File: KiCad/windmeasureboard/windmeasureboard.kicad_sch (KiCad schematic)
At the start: 9 parts, among them J1 ESQ-120-XX-X-D-XX, U1 ESP32-S2-DEVKITC-1, U2 LM1084ISX-5.0_NOPB

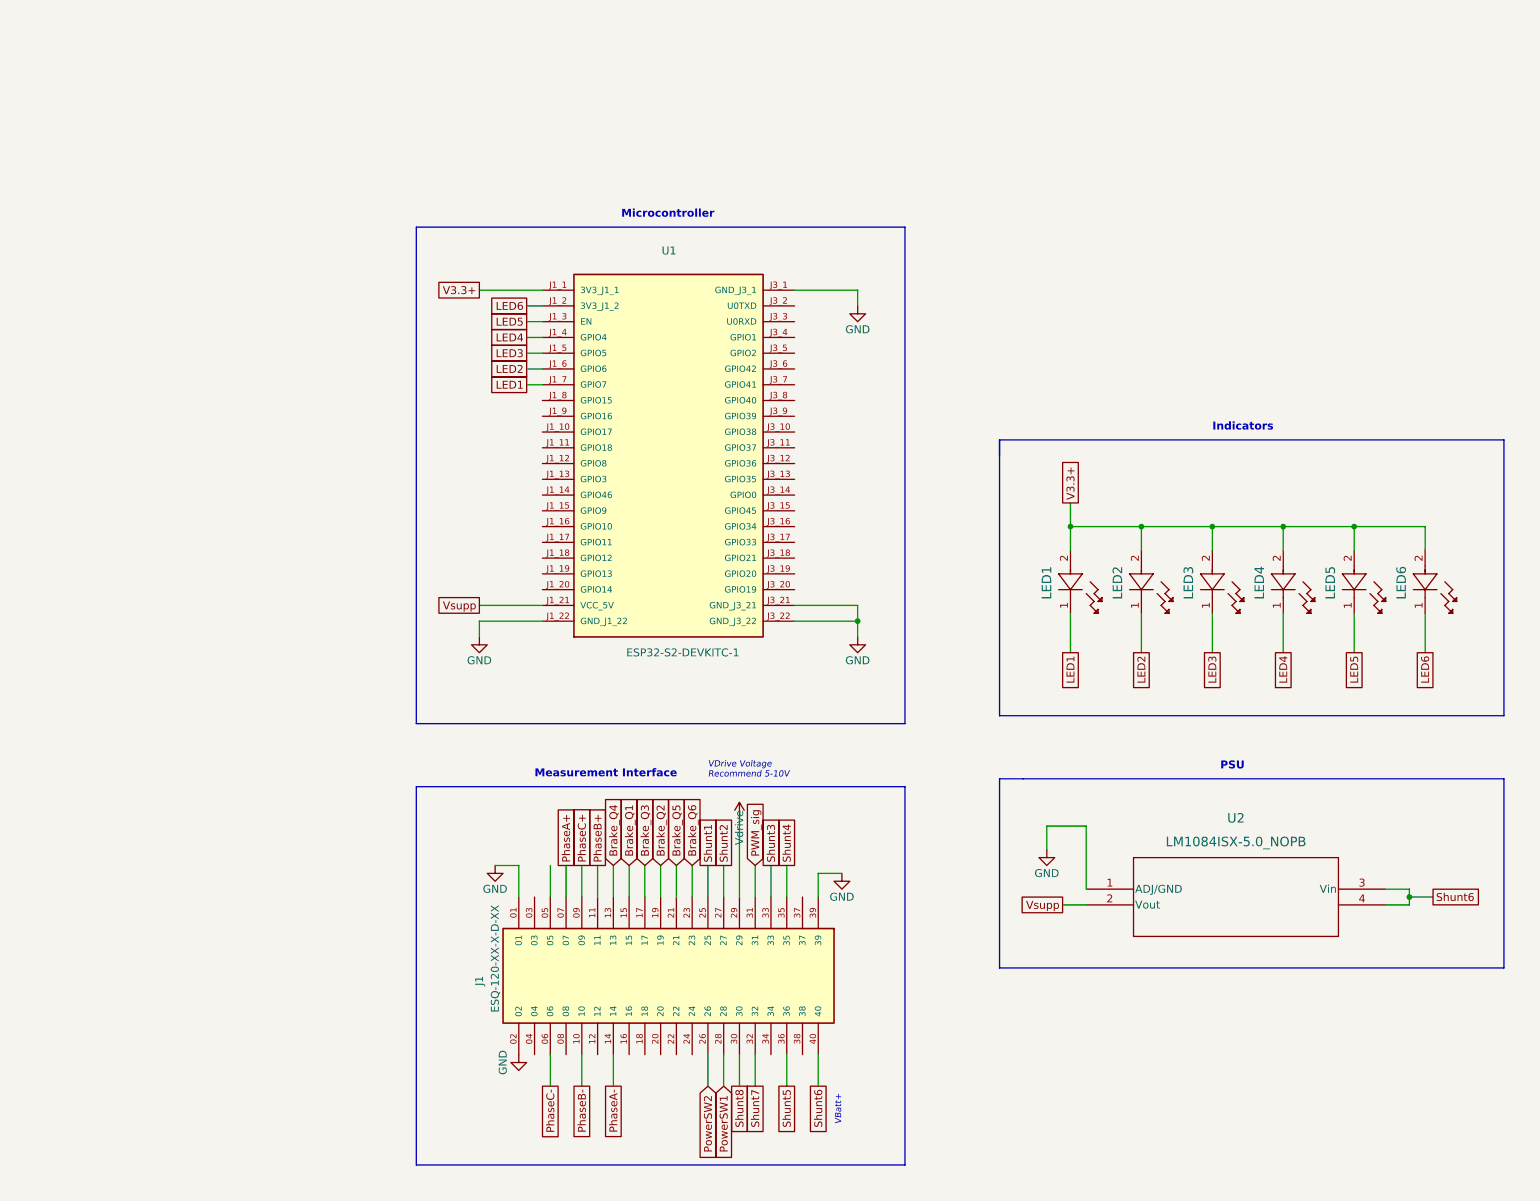
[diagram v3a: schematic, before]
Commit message: V1 Measure Board Finished
Also started manual data collection for turbine and started updating files to kicad V7
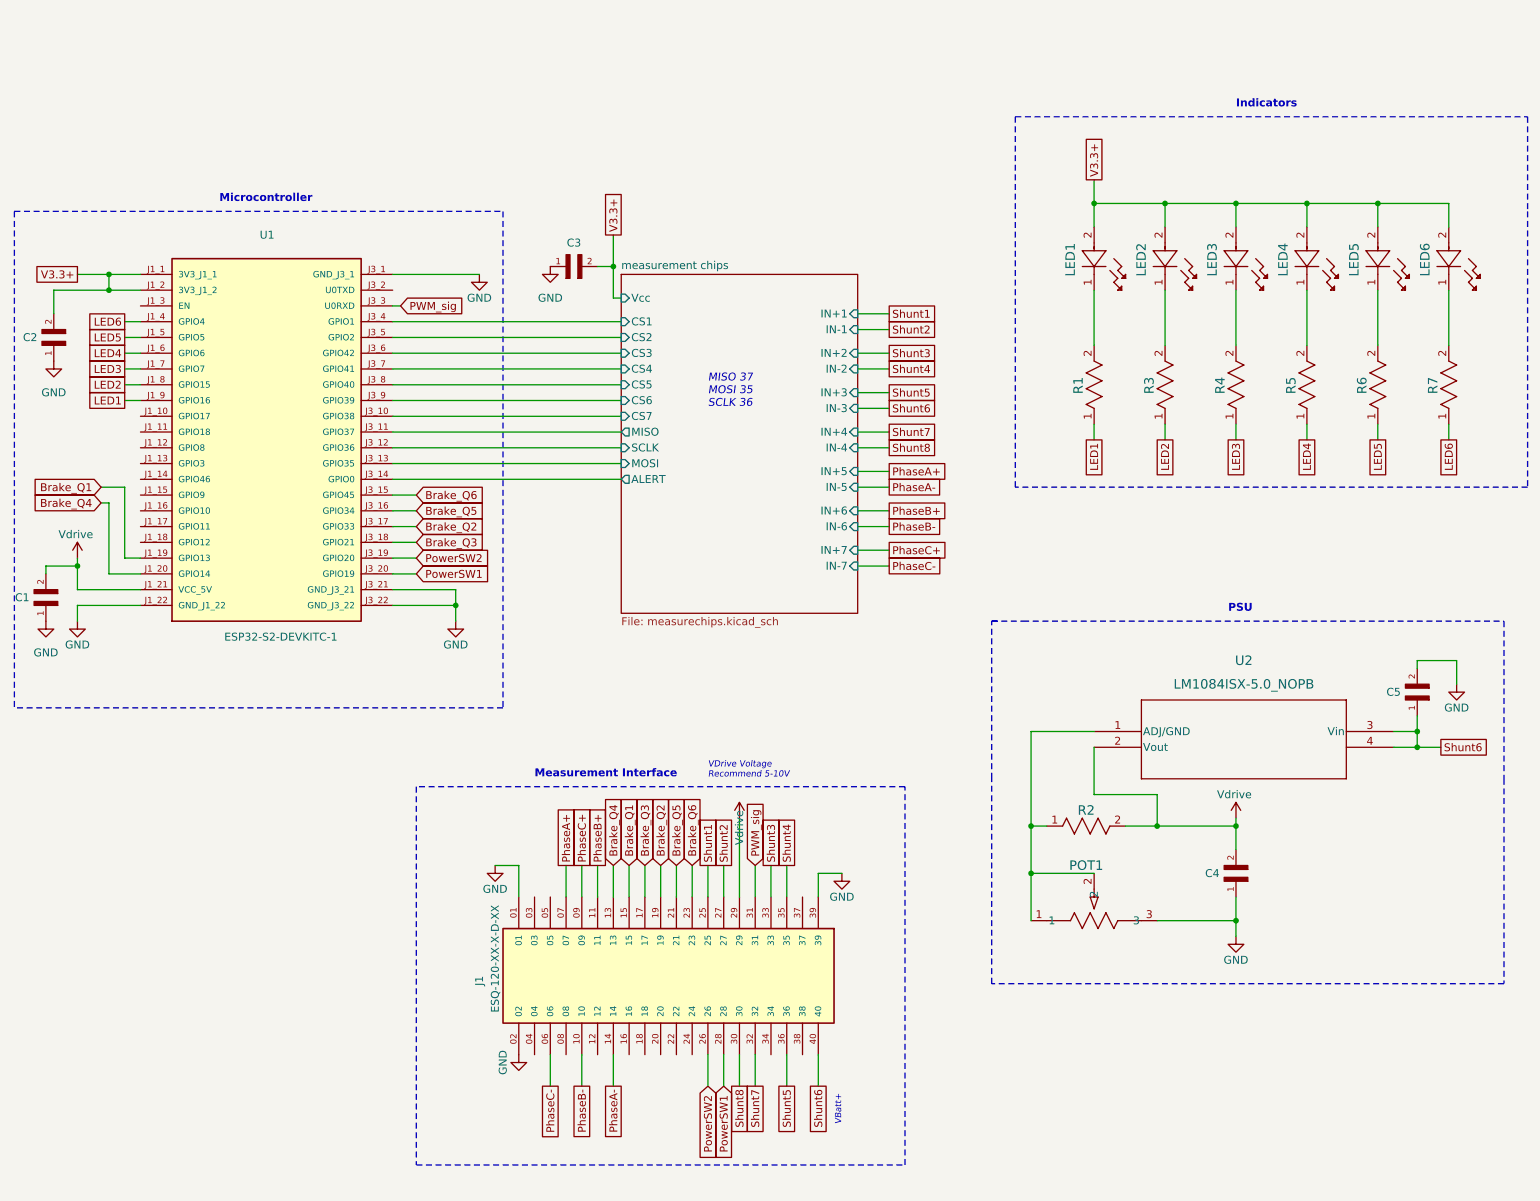
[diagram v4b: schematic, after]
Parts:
- added C1, C2, C3, C4, C5: GRM32EC72A106KE05L, footprints:CAPC3225X270N, symbol GRM32EC72A106KE05L:GRM32EC72A106KE05L
- added POT1: 3296Y-1-502LF, footprints:POT_3296Y, symbol 3296Y-1-502LF:3296Y-1-502LF
- added R1, R3, R4, R5, R6, R7: ERJXGNJ560Y, ERJXGN_RCD, symbol ERJXGNJ560Y:ERJXGNJ560Y
- added R2: CRCW04021K00FKED, footprints:RES_CRCW_0402, symbol CRCW04021K00FKED:CRCW04021K00FKED
- LED1, LED2, LED3, LED4, LED5, LED6: footprint LED_XZMG56W_SLD -> footprints:LED_XZMG56W_SLD
- U2: footprint TS3B -> footprints:TS3B
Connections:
- net Vsupp is gone; now on net Vdrive: U1.J1_21 (VCC_5V), U2.2 (Vout)
- net Brake_Q1: now also U1.J1_19 (GPIO13)
- net Brake_Q2: now also U1.J3_17 (GPIO33)
- net Brake_Q3: now also U1.J3_18 (GPIO21)
- net Brake_Q4: now also U1.J1_20 (GPIO14)
- net Brake_Q5: now also U1.J3_16 (GPIO34)
- net Brake_Q6: now also U1.J3_15 (GPIO45)
- net GND: now also C1.1, C2.1, C3.1, C4.1, C5.2, POT1.3; no longer U2.1 (ADJ/GND)
- net LED1: now also U1.J1_9 (GPIO16), R1.1; no longer LED1.1, U1.J1_7 (GPIO7)
- net LED2: now also U1.J1_8 (GPIO15), R3.1; no longer LED2.1, U1.J1_6 (GPIO6)
- net LED3: now also U1.J1_7 (GPIO7), R4.1; no longer LED3.1, U1.J1_5 (GPIO5)
- net LED4: now also U1.J1_6 (GPIO6), R5.1; no longer LED4.1, U1.J1_4 (GPIO4)
- net LED5: now also U1.J1_5 (GPIO5), R6.1; no longer LED5.1, U1.J1_3 (EN)
- net LED6: now also U1.J1_4 (GPIO4), R7.1; no longer LED6.1, U1.J1_2 (3V3_J1_2)
- net PWM_sig: now also U1.J3_3 (U0RXD)
- net PowerSW1: now also U1.J3_20 (GPIO19)
- net PowerSW2: now also U1.J3_19 (GPIO20)
- net Shunt6: now also C5.1
- net V3.3+: now also U1.J1_2 (3V3_J1_2), C2.2, C3.2
- net Vdrive: now also C1.2, C4.2, R2.2
- net measurement chips/CS7: now reaches U1.J3_10 (GPIO38)
- net measurement chips/MISO: now reaches U1.J3_11 (GPIO37)
- net measurement chips/SCLK: now reaches U1.J3_12 (GPIO36)
- net measurement chips/MOSI: now reaches U1.J3_13 (GPIO35)
- net measurement chips/ALERT: now reaches U1.J3_14 (GPIO0)
- net measurement chips/CS1: now reaches U1.J3_4 (GPIO1)
- net measurement chips/CS2: now reaches U1.J3_5 (GPIO2)
- net measurement chips/CS3: now reaches U1.J3_6 (GPIO42)
- net measurement chips/CS4: now reaches U1.J3_7 (GPIO41)
- net measurement chips/CS5: now reaches U1.J3_8 (GPIO40)
- net measurement chips/CS6: now reaches U1.J3_9 (GPIO39)
- new net: LED5.1, R6.2
- new net: LED2.1, R3.2
- new net: LED3.1, R4.2
- new net: POT1.1, POT1.2, R2.1, U2.1 (ADJ/GND)
- new net: LED6.1, R7.2
- new net: LED4.1, R5.2
- new net: LED1.1, R1.2
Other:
- added sheet measurement chips (measurechips.kicad_sch)
- note added: "MISO 37 MOSI 35 SCLK 36"
- moved on the sheet: LED1, LED2, LED3, LED4, LED5, LED6, U1, U2

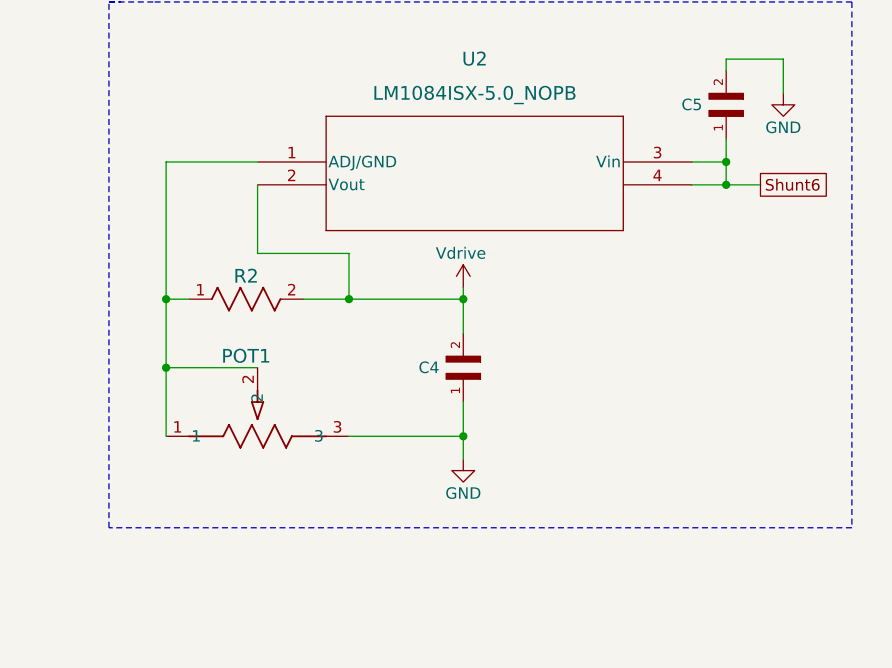
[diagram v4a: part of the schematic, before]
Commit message: started V2 WMB
fixed PSU issue
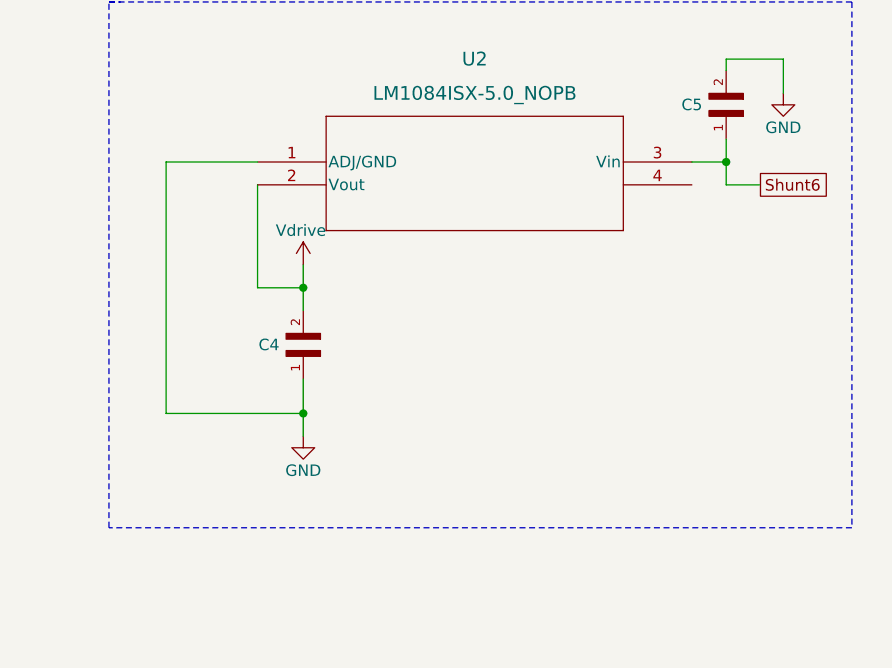
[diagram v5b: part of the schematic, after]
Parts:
- removed POT1: 3296Y-1-502LF, footprints:POT_3296Y, symbol 3296Y-1-502LF:3296Y-1-502LF
- removed R2: CRCW04021K00FKED, footprints:RES_CRCW_0402, symbol CRCW04021K00FKED:CRCW04021K00FKED
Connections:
- net GND: now also U2.1 (ADJ/GND)
- net Shunt6: no longer U2.4
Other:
- moved on the sheet: C4

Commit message: Finished WMB V2.1
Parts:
- removed R1, R3, R4, R5, R6, R7: ERJXGNJ560Y, ERJXGN_RCD, symbol ERJXGNJ560Y:ERJXGNJ560Y
- added R1, R2, R3, R4, R5, R6: CPA2512E56R0FS-T10, footprints:RESC6332X80N, symbol CPA2512E56R0FS-T10:CPA2512E56R0FS-T10
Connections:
- net Brake_Q5 is gone; now on net Brake_Q4: J1.21, U1.J3_16 (GPIO34)
- net measurement chips/MISO is gone; now on net MISO: U1.J3_11 (GPIO37)
- net measurement chips/MOSI is gone; now on net MOSI: U1.J3_13 (GPIO35)
- net measurement chips/SCLK is gone; now on net SCLK: U1.J3_12 (GPIO36)
- net Brake_Q1: now also J1.17, J1.19, U1.J3_15 (GPIO45); no longer U1.J1_19 (GPIO13)
- net Brake_Q4: now also J1.23; no longer U1.J1_20 (GPIO14)
- net LED1: now also R1.1
- net LED2: now also R2.1
- net LED3: now also R3.1
- net LED4: now also R4.1
- net LED5: now also R5.1
- net LED6: now also R6.1
- net V3.3+: now also J1.37
- net at LED5.1: now also R5.2
- net at LED2.1: now also R2.2
- net at LED3.1: now also R3.2
- net at LED6.1: now also R6.2
- net at LED4.1: now also R4.2
- net at LED1.1: now also R1.2
- net GEN_CS: now reaches J1.16
- net GEN_CS: now also U1.J1_16 (GPIO10)
- net GEN_PWM: now reaches J1.18
- net GEN_PWM: now also U1.J1_17 (GPIO11)
- net MISO: now reaches J1.20
- net SCLK: now reaches J1.22
- net MOSI: now reaches J1.24
- net Brake_Q2: no longer names the net of U1.J3_17 (GPIO33)
- net Brake_Q2: no longer J1.19
- net Brake_Q3: no longer names the net of U1.J3_18 (GPIO21)
- net Brake_Q3: no longer J1.17
- removed net Brake_Q6: J1.23, U1.J3_15 (GPIO45)

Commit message: WMB 2.2 pushed and ordered
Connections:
- net Brake_Q1: now also U1.J3_16 (GPIO34); no longer U1.J3_15 (GPIO45)
- net Brake_Q4: now also U1.J3_17 (GPIO33); no longer U1.J3_16 (GPIO34)
- net MISO: now also U1.J3_12 (GPIO36); no longer U1.J3_11 (GPIO37)
- net MOSI: now also U1.J3_14 (GPIO0); no longer U1.J3_13 (GPIO35)
- net PWM_sig: now also U1.J3_4 (GPIO1); no longer U1.J3_3 (U0RXD)
- net SCLK: now also U1.J3_13 (GPIO35); no longer U1.J3_12 (GPIO36)
- net measurement chips/ALERT: now also U1.J3_15 (GPIO45); no longer U1.J3_14 (GPIO0)
- net measurement chips/CS1: now also U1.J3_5 (GPIO2); no longer U1.J3_4 (GPIO1)
- net measurement chips/CS2: now also U1.J3_6 (GPIO42); no longer U1.J3_5 (GPIO2)
- net measurement chips/CS3: now also U1.J3_7 (GPIO41); no longer U1.J3_6 (GPIO42)
- net measurement chips/CS4: now also U1.J3_8 (GPIO40); no longer U1.J3_7 (GPIO41)
- net measurement chips/CS5: now also U1.J3_9 (GPIO39); no longer U1.J3_8 (GPIO40)
- net measurement chips/CS6: now also U1.J3_10 (GPIO38); no longer U1.J3_9 (GPIO39)
- net measurement chips/CS7: now also U1.J3_11 (GPIO37); no longer U1.J3_10 (GPIO38)
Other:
- moved on the sheet: C3
